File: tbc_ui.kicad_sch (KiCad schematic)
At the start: 28 parts

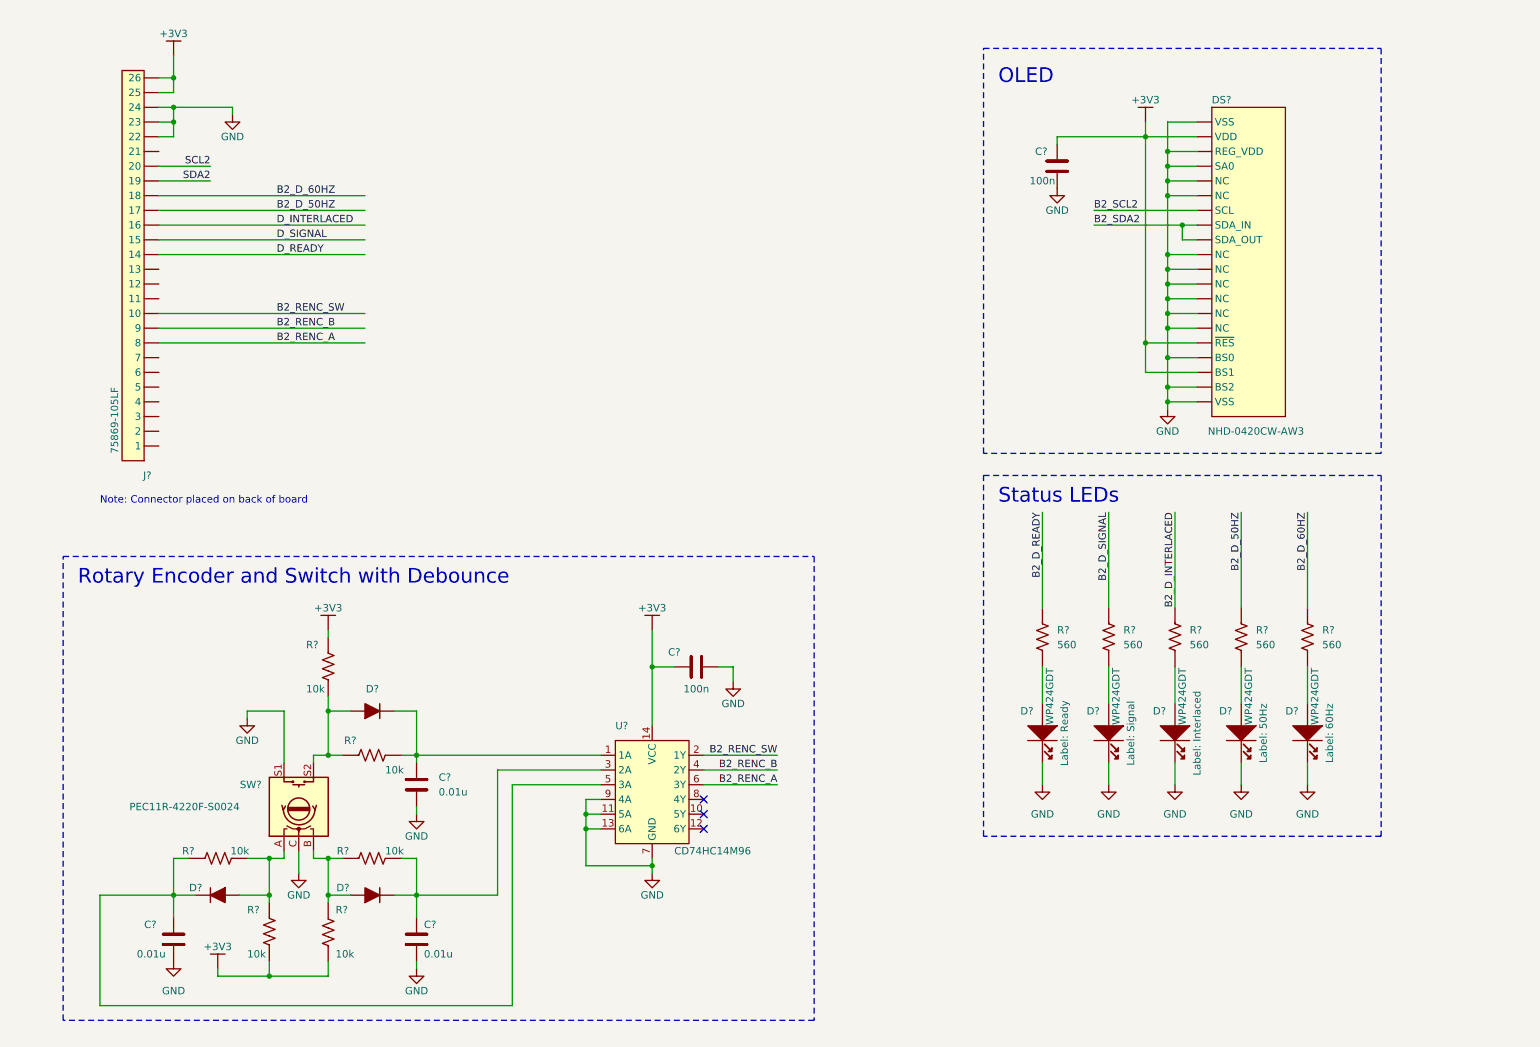
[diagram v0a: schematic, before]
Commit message: annotated and DRC'd schematic
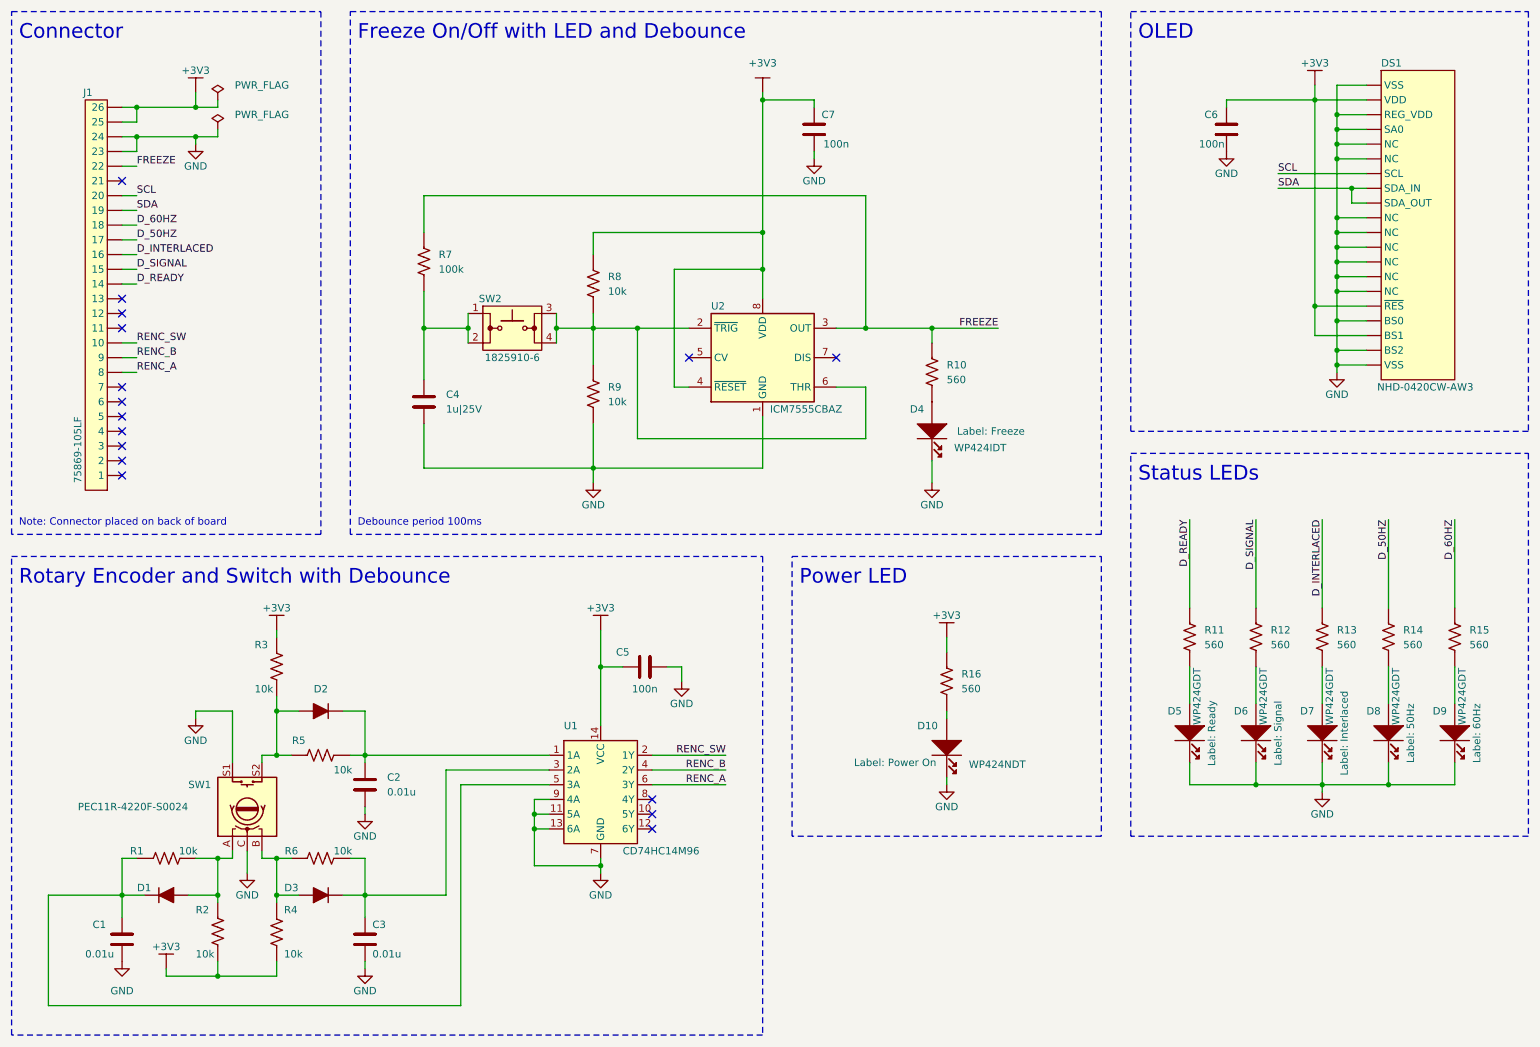
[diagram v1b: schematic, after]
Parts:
- added C4: 1u|25V, symbol tbc:GCJ188R71E105KA01D
- added C7: 100n, symbol tbc:GCJ188R71H104KA12D
- added D10: WP424NDT, symbol tbc:WP424NDT
- added D4: WP424IDT, symbol tbc:WP424IDT
- added R10, R16: 560, symbol tbc:RC0603FR-07560RL
- added R7: 100k, symbol tbc:RC0603FR-07100KL
- added R8, R9: 10k, symbol tbc:RC0603FR-0710KL
- added SW2: 1825910-6, symbol tbc:1825910-6
- added U2: ICM7555CBAZ, symbol tbc:ICM7555CBAZ
- gave numbers to parts that had none: 28
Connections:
- net B2_D_INTERLACED is gone; now on net D_INTERLACED: R13.2
- net B2_D_READY is gone; now on net D_READY: R11.2
- net B2_D_SIGNAL is gone; now on net D_SIGNAL: R12.2
- net SCL2 is gone; now on net SCL: J1.20
- net SDA2 is gone; now on net SDA: J1.19
- net +3V3: now also C7.2, R16.2, R8.2, U2.4 (~{RESET}), U2.8 (VDD)
- net GND: now also C4.1, C7.1, D10.1 (Cathode), D4.1 (Cathode), R9.1, U2.1 (GND); no longer J1.22
- net B2_D_50HZ renamed D_50HZ
- net B2_D_60HZ renamed D_60HZ
- net B2_RENC_A renamed RENC_A
- net B2_RENC_B renamed RENC_B
- net B2_RENC_SW renamed RENC_SW
- net B2_SCL2 renamed SCL
- net B2_SDA2 renamed SDA
- new net: D4.2 (Anode), R10.1
- new net: D10.2 (Anode), R16.1
- new net: C4.2, R7.1, SW2.1, SW2.2
- new net: R8.1, R9.2, SW2.3, SW2.4, U2.2 (~{TRIG}), U2.6 (THR)
- new net FREEZE: J1.22, R10.2, R7.2, U2.3 (OUT)
- no-connect marks 3 -> 16
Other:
- note added: "Connector"
- note added: "Debounce period 100ms"
- note added: "Freeze On/Off with LED and Debounce"
- note added: "Power LED"
- moved on the sheet: C1, C2, C3, C5, C6, D1, D2, D3, D5, D6, D7, D8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

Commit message: switched out tactile switch
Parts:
- SW2: value 1825910-6 -> TL1100F160Q; symbol tbc:1825910-6 -> tbc:TL1100F160Q; Mouser 650-1825910-6 -> 612-TL1100
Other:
- note added: "C&K F0201 is the switch cap part"
- company: (none) -> Wavelet Engineering Pty Ltd (ACN 159 717 665)
- title: (none) -> Time Base Corrector and Video Scaler - User Interface
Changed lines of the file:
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@@
 (kicad_sch (version 20230121) (generator eeschema)
   (paper "A4")
+  (title_block
+    (title "Time Base Corrector and Video Scaler - User Interface")
+    (date "2024-01-25")
+    (rev "1")
+    (company "Wavelet Engineering Pty Ltd (ACN 159 717 665)")
+    (comment 1 "https://github.com/philmcm/tbc-ui")
+    (comment 3 "Enhancements © 2024 Phil McMillan")
+    (comment 4 "Original TBC circuit design © 2001 Marcus Gunnarsson")
+  )
   (junction (at 246.38 57.15) (diameter 0) (color 0 0 0 0)
   )
@@
     (effects (font (size 2.54 2.54)) (justify left bottom))
   )
+  (text "C&K F0201 is the switch cap part" (at 77.47 102.87 0)
+    (effects (font (size 1.27 1.27)) (justify left bottom))
+  )
   (text "Note: Connector placed on back of board" (at 19.05 105.41 0)
     (effects (font (size 1.27 1.27)) (justify left bottom))
@@
     )
   )
-  (symbol (lib_id "tbc:1825910-6") (at 104.14 71.12 0) (unit 1)
+  (symbol (lib_id "tbc:TL1100F160Q") (at 104.14 71.12 0) (unit 1)
     (in_bom yes) (on_board yes) (dnp no)
     (property "Reference" "SW2" (at 100.33 66.04 0)
       (effects (font (size 1.27 1.27)))
     )
-    (property "Value" "1825910-6" (at 104.14 76.2 0)
+    (property "Value" "TL1100F160Q" (at 104.14 76.2 0)
       (effects (font (size 1.27 1.27)))
     )
@@
       (effects (font (size 1.27 1.27)) hide)
     )
-    (property "Datasheet" "http://www.te.com/commerce/DocumentDelivery/DDEController?Action=srchrtrv&DocNm=1825910&DocType=Customer+Drawing&DocLang=English" (at 104.14 78.74 0) (show_name)
-      (effects (font (size 1.27 1.27)) hide)
-    )
-    (property "Mouser" "650-1825910-6" (at 104.14 66.04 0) (show_name)
-      (effects (font (size 1.27 1.27)) hide)
-    )
+    (property "Datasheet" "https://au.mouser.com/datasheet/2/140/TL1100-3305406.pdf" (at 104.14 78.74 0) (show_name)
+      (effects (font (size 1.27 1.27)) hide)
+    )
+    (property "Mouser" " 612-TL1100" (at 104.14 66.04 0) (show_name)
+      (effects (font (size 1.27 1.27)) hide)
+    )
